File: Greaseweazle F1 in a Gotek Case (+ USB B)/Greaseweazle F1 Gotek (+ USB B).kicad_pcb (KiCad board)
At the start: 2 copper layers, 111.6 x 85.3 mm, 66 parts, among them CN1 Floppy Data, J1 PinHeader_1x04_P2.54mm_Vertic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, J1 USB A, J2 Floppy Power, J3 Programming Port, J4 USB B, SW1 Reset, U1 Blue Pill

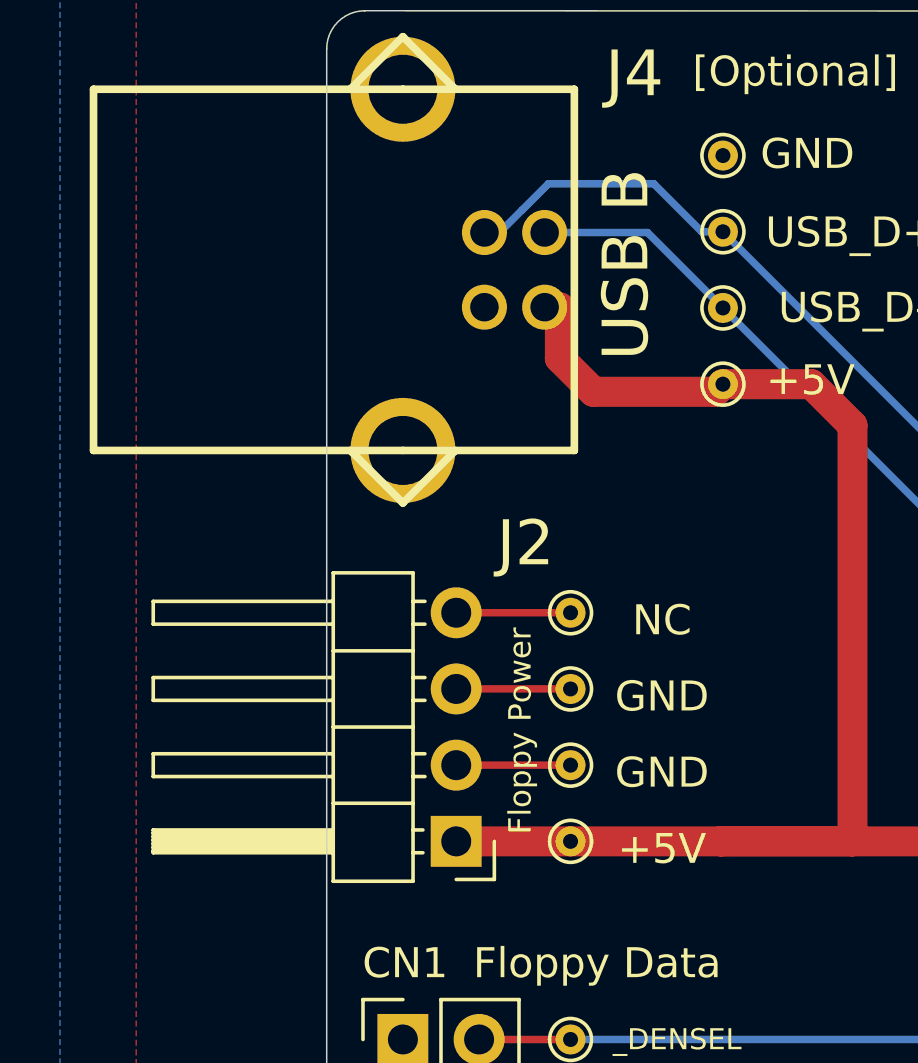
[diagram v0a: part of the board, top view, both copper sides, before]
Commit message: Shifted floppy power, and corrected some USB B port traces
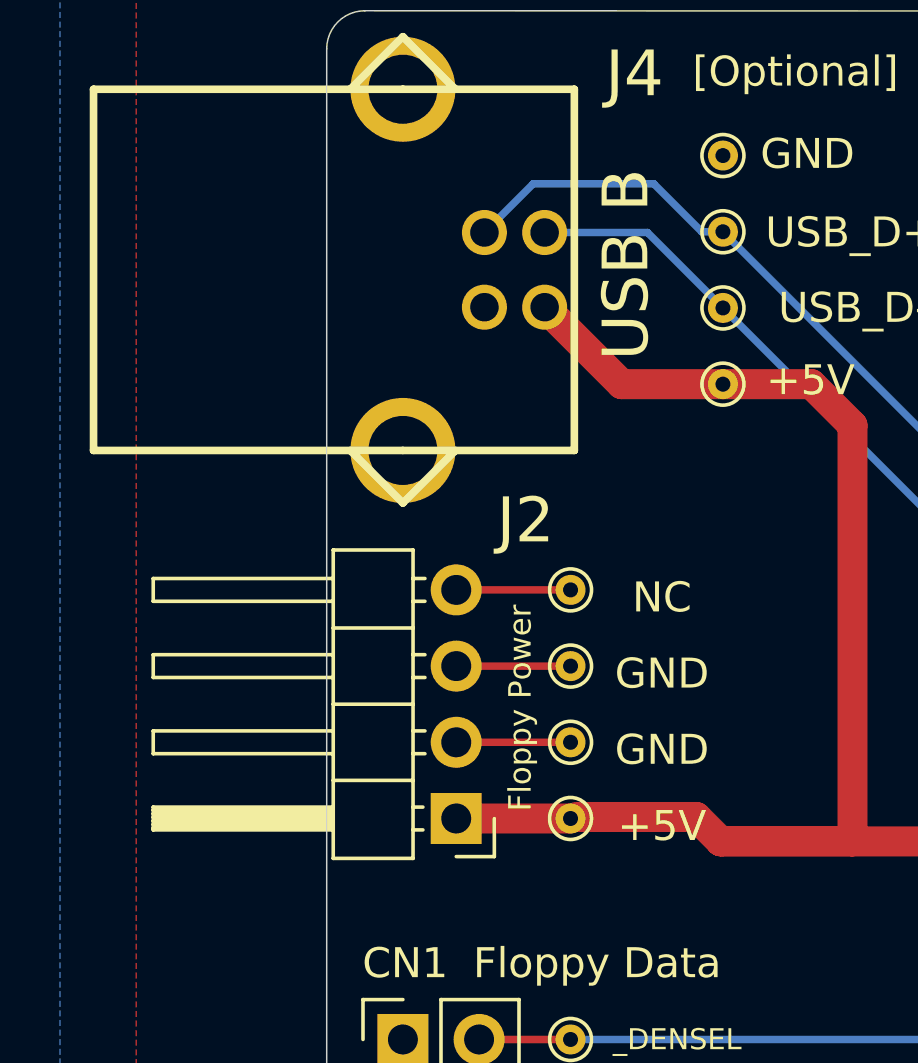
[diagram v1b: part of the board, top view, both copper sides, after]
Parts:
- moved ? 0.76 mm to (103.4, 59.9)
- moved ? 0.76 mm to (103.4, 62.5)
- moved ? 0.76 mm to (103.4, 65.0)
- moved J2 0.76 mm to (99.6, 65.0)
- moved ? 0.76 mm to (103.4, 57.4)
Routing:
- net Net-(J1-Pad3): track 134.9 -> 135.4 mm
